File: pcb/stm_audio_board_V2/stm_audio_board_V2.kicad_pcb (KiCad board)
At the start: 4 copper layers, 141 parts, among them J1 Power conn, J10 Conn_01x03_taptempo, J2 STlink, J3 Audio_sig, J4 Conn_01x10_pots_internal, J5 SPI, J6 Conn_01x03_pot_ext, J7 GuitarIN, J8 GuitarOUT_R, J9 GuitarOUT_L, SW1 SW_SPST, U1 STM32H730VBTx, U2 AMS1117-3.3, U4 OP275, U5 AMS1117-3.3, U7 MCP1703Ax-500xxDB, U9 L7809, Y1 Crystal_GND24, Y2 X1E0000210132

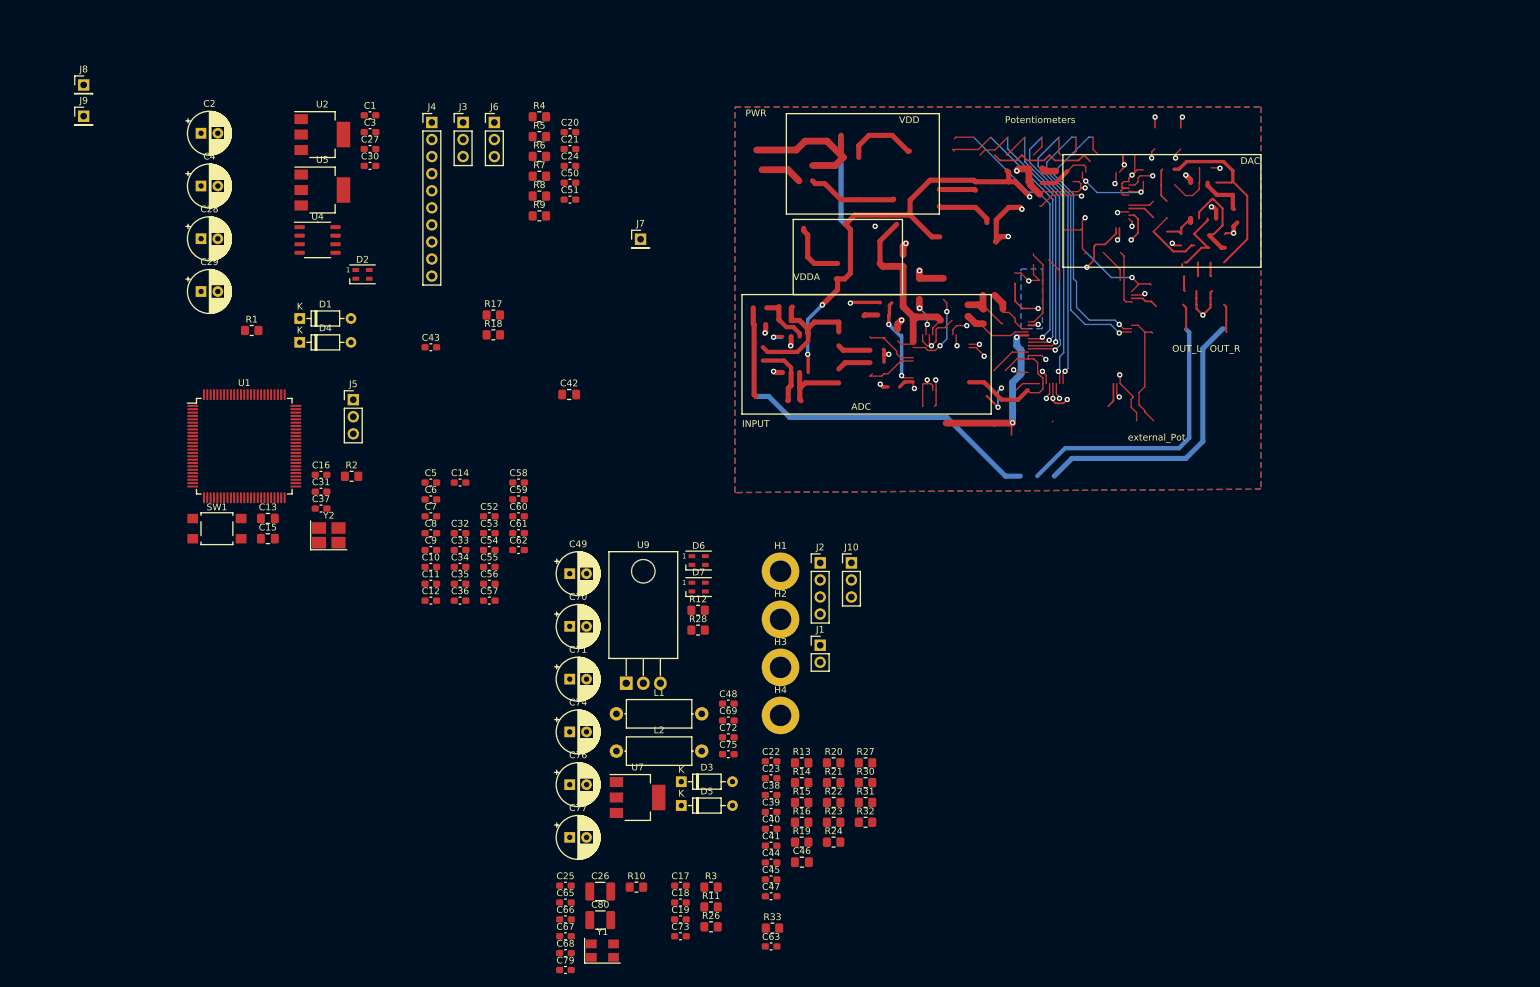
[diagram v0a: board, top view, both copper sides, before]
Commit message: PCB design started INPUT and OUTPUT stage done, codec placed
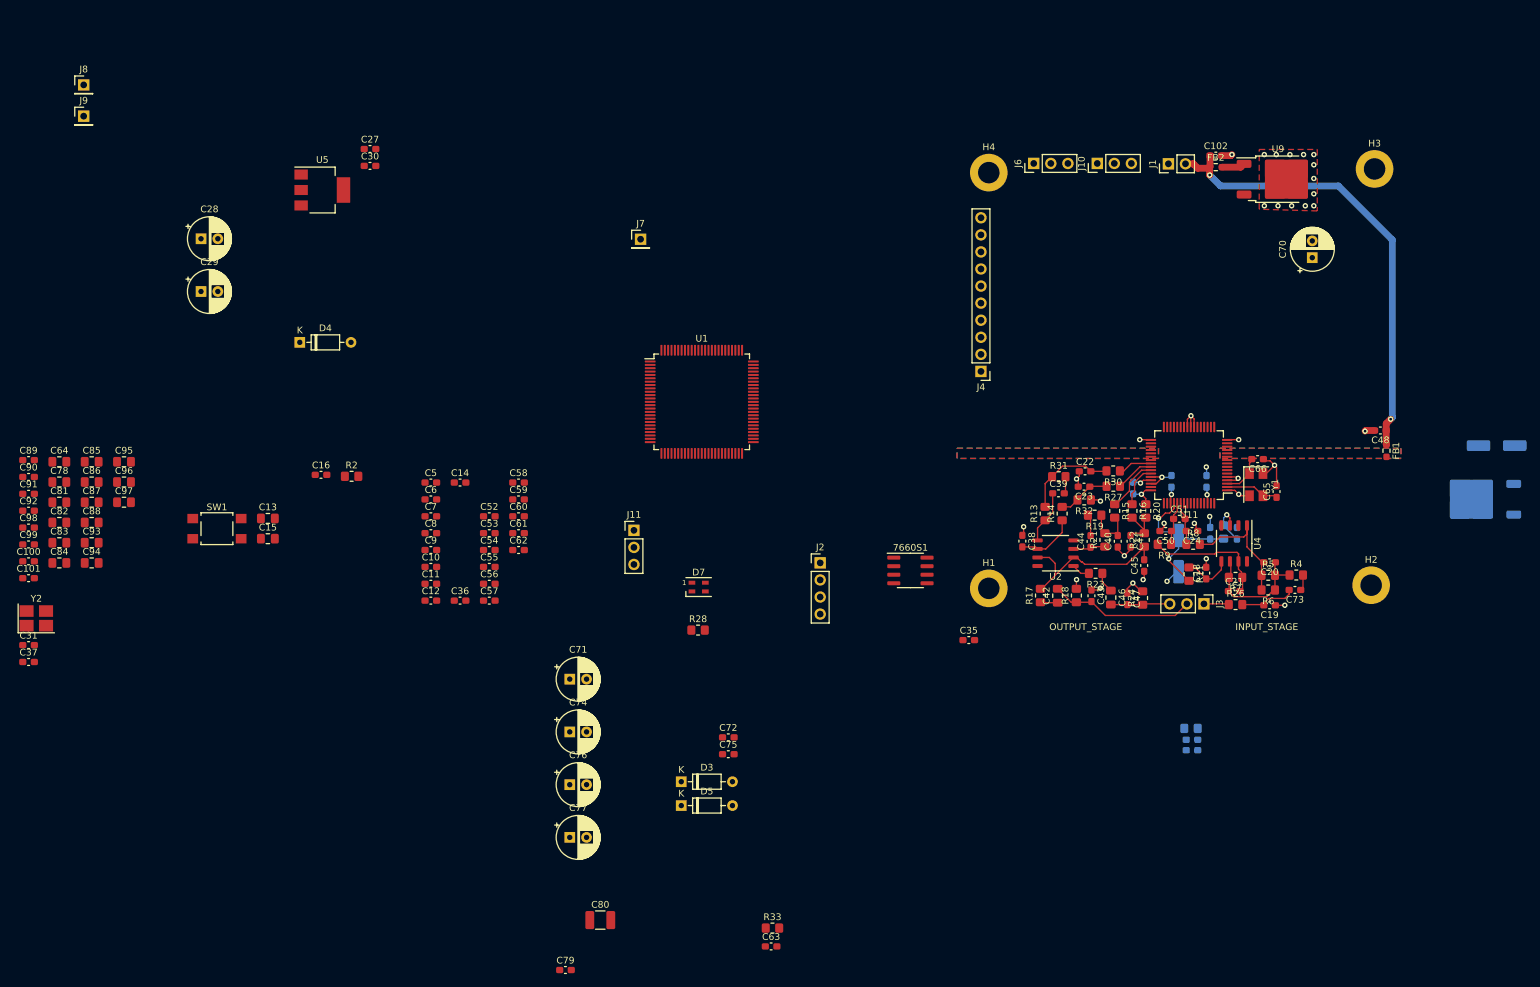
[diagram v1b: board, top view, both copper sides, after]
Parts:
- removed C1, C3, C69: 100nF, Capacitor_SMD:C_0603_1608Metric_Pad1.08x0.95mm_HandSolder
- removed C2: 1uF, Capacitor_THT:CP_Radial_D6.3mm_P2.50mm
- removed C4: 100uF, Capacitor_THT:CP_Radial_D6.3mm_P2.50mm
- removed D1: 1N4148, Diode_THT:D_DO-35_SOD27_P7.62mm_Horizontal
- removed D2, D6: LED, LED_SMD:LED_SK6805_PLCC4_2.4x2.7mm_P1.3mm
- removed J5: SPI, Connector_PinHeader_2.54mm:PinHeader_1x03_P2.54mm_Vertical
- removed L1, L2: 10 uH|0,5R, Inductor_THT:L_Axial_L9.5mm_D4.0mm_P12.70mm_Horizontal_Fastron_SMCC
- removed R1: 330R, Resistor_SMD:R_0805_2012Metric_Pad1.20x1.40mm_HandSolder
- removed R12: 10k, Resistor_SMD:R_0805_2012Metric_Pad1.20x1.40mm_HandSolder
- removed U7: MCP1703Ax-500xxDB, Package_TO_SOT_SMD:SOT-223-3_TabPin2
- added 7660S1: ~, Package_SO:SOIC-8_3.9x4.9mm_P1.27mm, F.Cu at (175.9, 109.6)
- added C100: 100nF, Capacitor_SMD:C_0603_1608Metric_Pad1.08x0.95mm_HandSolder, F.Cu at (44.7, 108.3)
- added C101: 100nF, Capacitor_SMD:C_0603_1608Metric_Pad1.08x0.95mm_HandSolder, F.Cu at (44.7, 110.8)
- added C102: 100nF, Capacitor_SMD:C_0603_1608Metric_Pad1.08x0.95mm_HandSolder, F.Cu at (221.4, 47.9)
- added C64: 47uF, Capacitor_SMD:C_0805_2012Metric_Pad1.18x1.45mm_HandSolder, F.Cu at (49.3, 93.5)
- added C78: 47uF, Capacitor_SMD:C_0805_2012Metric_Pad1.18x1.45mm_HandSolder, F.Cu at (49.3, 96.5)
- added C81: 47uF, Capacitor_SMD:C_0805_2012Metric_Pad1.18x1.45mm_HandSolder, F.Cu at (49.3, 99.5)
- added C82: 47uF, Capacitor_SMD:C_0805_2012Metric_Pad1.18x1.45mm_HandSolder, F.Cu at (49.3, 102.5)
- added C83: 47uF, Capacitor_SMD:C_0805_2012Metric_Pad1.18x1.45mm_HandSolder, F.Cu at (49.3, 105.5)
- added C84: 47uF, Capacitor_SMD:C_0805_2012Metric_Pad1.18x1.45mm_HandSolder, F.Cu at (49.3, 108.5)
- added C85: 47uF, Capacitor_SMD:C_0805_2012Metric_Pad1.18x1.45mm_HandSolder, F.Cu at (54.1, 93.5)
- added C86: 47uF, Capacitor_SMD:C_0805_2012Metric_Pad1.18x1.45mm_HandSolder, F.Cu at (54.1, 96.5)
- added C87: 47uF, Capacitor_SMD:C_0805_2012Metric_Pad1.18x1.45mm_HandSolder, F.Cu at (54.1, 99.5)
- added C88: 47uF, Capacitor_SMD:C_0805_2012Metric_Pad1.18x1.45mm_HandSolder, F.Cu at (54.1, 102.5)
- added C89: 100nF, Capacitor_SMD:C_0603_1608Metric_Pad1.08x0.95mm_HandSolder, F.Cu at (44.7, 93.2)
- added C90: 100nF, Capacitor_SMD:C_0603_1608Metric_Pad1.08x0.95mm_HandSolder, F.Cu at (44.7, 95.7)
- added C91: 100nF, Capacitor_SMD:C_0603_1608Metric_Pad1.08x0.95mm_HandSolder, F.Cu at (44.7, 98.2)
- added C92: 100nF, Capacitor_SMD:C_0603_1608Metric_Pad1.08x0.95mm_HandSolder, F.Cu at (44.7, 100.7)
- added C93: 47uF, Capacitor_SMD:C_0805_2012Metric_Pad1.18x1.45mm_HandSolder, F.Cu at (54.1, 105.5)
- added C94: 47uF, Capacitor_SMD:C_0805_2012Metric_Pad1.18x1.45mm_HandSolder, F.Cu at (54.1, 108.5)
- added C95: 47uF, Capacitor_SMD:C_0805_2012Metric_Pad1.18x1.45mm_HandSolder, F.Cu at (58.9, 93.5)
- added C96: 47uF, Capacitor_SMD:C_0805_2012Metric_Pad1.18x1.45mm_HandSolder, F.Cu at (58.9, 96.5)
- added C97: 47uF, Capacitor_SMD:C_0805_2012Metric_Pad1.18x1.45mm_HandSolder, F.Cu at (58.9, 99.5)
- added C98: 100nF, Capacitor_SMD:C_0603_1608Metric_Pad1.08x0.95mm_HandSolder, F.Cu at (44.7, 103.3)
- added C99: 100nF, Capacitor_SMD:C_0603_1608Metric_Pad1.08x0.95mm_HandSolder, F.Cu at (44.7, 105.8)
- added FB1: FerriteBead, Resistor_SMD:R_0603_1608Metric_Pad0.98x0.95mm_HandSolder, F.Cu at (246.8, 91.8)
- added FB2: FerriteBead, Resistor_SMD:R_0603_1608Metric_Pad0.98x0.95mm_HandSolder, F.Cu at (221.4, 49.6)
- added J11: SPI, Connector_PinHeader_2.54mm:PinHeader_1x03_P2.54mm_Vertical, F.Cu at (134.8, 103.7)
- added U11: ~, Package_QFP:LQFP-64_10x10mm_P0.5mm, F.Cu at (217.4, 94.0)
- added U8: L78M09CDT, Package_TO_SOT_SMD:TO-252-2, B.Cu at (260.7, 99.0)
- C17, C25, C32, C33, C34, C67, C68, R10, R3: moved to B.Cu
- C26: footprint Capacitor_SMD:C_1210_3225Metric_Pad1.33x2.70mm_HandSolder -> Capacitor_SMD:CP_Elec_6.3x7.7; moved to B.Cu
- C49: footprint Capacitor_THT:CP_Radial_D6.3mm_P2.50mm -> Capacitor_SMD:CP_Elec_6.3x7.7; moved to B.Cu
- C71, C74: value 1uF -> 47uf
- U2: value AMS1117-3.3 -> OP275; footprint Package_TO_SOT_SMD:SOT-223-3_TabPin2 -> Package_SO:SSOP-8_3.9x5.05mm_P1.27mm
- U9: value L7809 -> LF33_TO252; footprint Package_TO_SOT_THT:TO-220-3_Horizontal_TabDown -> Package_TO_SOT_SMD:TO-252-2
- moved U4 143.7 mm to (224.1, 105.6), turned to -90 degrees
- moved C49 139.2 mm to (263.2, 91.1), turned to 180 degrees
- moved R4 131.7 mm to (233.4, 110.3)
- moved J3 131.5 mm to (219.6, 114.6), turned to -90 degrees
- moved R5 126.6 mm to (229.2, 110.4)
- moved R6 126.2 mm to (229.2, 112.5), turned to 180 degrees
- moved U2 125.6 mm to (197.5, 107.1), turned to 180 degrees
- moved C66 123.7 mm to (227.6, 93.1), turned to 180 degrees
- moved C70 123.4 mm to (235.7, 63.1), turned to 90 degrees
- moved U9 122.6 mm to (230.6, 51.4)
- moved C20 122.2 mm to (229.4, 108.4), turned to 180 degrees
- moved C65 122.2 mm to (230.4, 97.9), turned to 90 degrees
- moved R7 119.6 mm to (224.3, 110.7), turned to 180 degrees
- moved Y1 119.5 mm to (227.4, 96.9), turned to -90 degrees
- moved C21 118.7 mm to (224.1, 112.7)
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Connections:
- C27 pad 1: Net-(D4-K) -> +9V
- C28 pad 1: Net-(D4-K) -> +9V
- C31 pad 2: Net-(U1-PH0) -> OSC0
- C32 pad 2: GNDA -> GND
- C33 pad 2: GNDA -> GND
- C34 pad 2: GNDA -> GND
- C35 pad 2: GNDA -> GND
- C36 pad 2: GNDA -> GND
- C37 pad 2: Net-(U1-PH1) -> OSC1
- C38 pad 2: Net-(U6A--) -> Net-(U2B--)
- C39 pad 1: Net-(U6A-+) -> Net-(U2B-+)
- C44 pad 1: Net-(U3B-+) -> Net-(U2A-+)
- C45 pad 2: Net-(U3B--) -> Net-(U2A--)
- C48 pad 1: Net-(D3-K) -> PWR_INPUT_12V-18V
- C52 pad 2: GNDA -> GND
- C53 pad 2: GNDA -> GND
- C70 pad 1: +9V -> Net-(D5-K)
- C71 pad 1: +5V -> +3.3V
- C72 pad 1: +5V -> +3.3V
- D4 pad 1: Net-(D4-K) -> +9V
- D5 pad 1: +9V -> Net-(D5-K)
- D5 pad 2: +5V -> +3.3V
- J1 pad 2: PWR_INPUT_9-18V -> PWR_INPUT_12V-18V
- R13 pad 1: Net-(U6A-+) -> Net-(U2B-+)
- R14 pad 1: Net-(U6A--) -> Net-(U2B--)
- R21 pad 1: Net-(U3B-+) -> Net-(U2A-+)
- R22 pad 1: Net-(U3B--) -> Net-(U2A--)
- U1 pad 12: Net-(U1-PH0) -> OSC0
- U1 pad 13: Net-(U1-PH1) -> OSC1
- U2 pad 1: GND -> Net-(R23-Pad2)
- U2 pad 2: +3.3V -> Net-(U2A--)
- U2 pad 3: +5V -> Net-(U2A-+)
- U5 pad 3: Net-(D4-K) -> +9V
- U9 pad 1: Net-(D3-K) -> Net-(D5-K)
- U9 pad 3: +9V -> +3.3V
- Y2 pad 1: Net-(U1-PH1) -> OSC0
- Y2 pad 3: Net-(U1-PH0) -> OSC1
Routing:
- net (no net): track 1249.0 -> 0.00 mm, vias 42 -> 0
- net VDD: track 155.2 -> 0.00 mm, vias 7 -> 0
- net GNDA: track 82.4 -> 0.00 mm, vias 20 -> 0
- net PWR_INPUT_12V-18V: track 0.00 -> 68.9 mm, vias 0 -> 2
- net +3.3VA: track 63.6 -> 7.52 mm, vias 6 -> 3
- net AD1939_CM: track 0.00 -> 24.5 mm, vias 0 -> 2
- net GUITAR_OUT_L/MONO: track 0.00 -> 21.7 mm
- net Net-(C40-Pad2): track 28.3 -> 7.33 mm
- net Net-(C20-Pad2): track 0.00 -> 19.7 mm
- net Net-(C21-Pad2): track 0.00 -> 18.4 mm
- net GND: track 80.1 -> 64.6 mm, vias 6 -> 38
- net Net-(C22-Pad2): track 0.00 -> 14.0 mm
- net Net-(U2A--): track 0.00 -> 13.4 mm
- net Net-(R17-Pad2): track 0.00 -> 11.9 mm
- net Net-(U1-PH1): track 10.2 -> 0.00 mm
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- added copper zone on B.Cu, net (none)
- added copper zone on F.Cu, net (none)
- added copper zone on In1.Cu, net (none)
- added copper zone on In2.Cu, net (none)
- added copper zone on In1.Cu, net GND
- removed copper zone on In2.Cu, net +3.3VA
- removed copper zone on B.Cu, net GNDA
- removed copper zone on B.Cu, net VDD
- removed copper zone on In1.Cu, net VDD
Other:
- board text added: "INPUT_STAGE"
- board text added: "OUTPUT_STAGE"
- board text removed: "ADC"
- board text removed: "DAC"
- board text removed: "INPUT"
- board text removed: "OUT_L"
- board text removed: "OUT_R"
- board text removed: "PWR"
- board text removed: "Potentiometers"
- board text removed: "VDD"
- board text removed: "VDDA"
- board text removed: "external_Pot"

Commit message: Update #auto_saved_files#, Connectors.kicad_sch, and 18 more files...
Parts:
- removed C100, C101, C35, C36, C52, C53, C91, C92, C98, C99: 100nF, Capacitor_SMD:C_0603_1608Metric_Pad1.08x0.95mm_HandSolder
- removed C84, C85, C86, C87, C88, C93, C94, C95, C96, C97: 47uF, Capacitor_SMD:C_0805_2012Metric_Pad1.18x1.45mm_HandSolder
- removed D4: 1N4148, Diode_THT:D_DO-35_SOD27_P7.62mm_Horizontal
- removed J7: GuitarIN, Connector_PinHeader_2.54mm:PinHeader_1x01_P2.54mm_Vertical
- removed J8: GuitarOUT_R, Connector_PinHeader_2.54mm:PinHeader_1x01_P2.54mm_Vertical
- removed J9: GuitarOUT_L, Connector_PinHeader_2.54mm:PinHeader_1x01_P2.54mm_Vertical
- C10, C11, C14, C15, C40, C41, C44, C45, C46, C47, C48, C6, C65, C66, C7, C76, C77, C79, C80, C9, FB1, R15, R16, R19, R2, R20, R21, R22, R23, R24, Y1: moved to B.Cu
- C28, C29: footprint Capacitor_THT:CP_Radial_D6.3mm_P2.50mm -> Capacitor_SMD:CP_Elec_6.3x7.7; moved to B.Cu
- C49: footprint Capacitor_SMD:CP_Elec_6.3x7.7 -> Capacitor_SMD:C_1206_3216Metric_Pad1.33x1.80mm_HandSolder
- moved C83 193.7 mm to (242.3, 88.3), turned to 90 degrees
- moved C82 190.5 mm to (239.3, 88.3), turned to 90 degrees
- moved C81 187.3 mm to (236.2, 88.3), turned to 90 degrees
- moved C90 185.0 mm to (229.4, 106.4)
- moved C78 184.1 mm to (233.2, 88.3), turned to 90 degrees
- moved C64 181.0 mm to (230.2, 88.3), turned to 90 degrees
- moved C31 165.2 mm to (200.2, 64.9)
- moved Y2 162.6 mm to (201.1, 68.4), turned to 180 degrees
- moved C37 161.8 mm to (197.1, 68.9), turned to -90 degrees
- moved C89 156.1 mm to (199.9, 110.2), turned to 90 degrees
- moved C13 148.6 mm to (224.6, 66.3)
- moved C15 142.1 mm to (219.0, 73.9)
- moved C12 130.2 mm to (224.1, 62.5), turned to -90 degrees
- moved C29 129.3 mm to (193.8, 106.7), turned to 180 degrees
- moved C74 127.2 mm to (250.2, 109.8)
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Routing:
- net +9V: track 0.00 -> 124.8 mm, vias 0 -> 4
- net +3.3V: track 0.00 -> 119.5 mm, vias 0 -> 7
- net GND: track 64.6 -> 147.1 mm, vias 38 -> 86
- net +3.3VA: track 7.52 -> 57.8 mm, vias 3 -> 4
- net -9V: track 0.00 -> 40.2 mm, vias 0 -> 2
- net /MCU/NRST: track 0.00 -> 33.6 mm, vias 0 -> 2
- net CLK: track 0.00 -> 31.0 mm, vias 0 -> 1
- net SWCLK: track 0.00 -> 31.0 mm, vias 0 -> 2
- net MISO: track 0.00 -> 26.7 mm, vias 0 -> 1
- net MOSI: track 0.00 -> 26.4 mm, vias 0 -> 1
- net SWDIO: track 0.00 -> 26.2 mm, vias 0 -> 1
- net DAC_EN: track 0.00 -> 17.3 mm
- net Net-(D5-K): track 3.50 -> 17.1 mm
- net AD1939_LF: track 0.00 -> 10.5 mm, vias 0 -> 1
- net AD1939_FILTR: track 0.00 -> 10.1 mm, vias 0 -> 1
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- added copper zone on B.Cu, net GND
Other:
- board text added: "U8"

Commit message: trace widening
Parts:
- added C100: 100nF, Capacitor_SMD:C_0603_1608Metric_Pad1.08x0.95mm_HandSolder, F.Cu at (153.1, 83.3)
- added C101: 100nF, Capacitor_SMD:C_0603_1608Metric_Pad1.08x0.95mm_HandSolder, F.Cu at (153.1, 85.8)
- added C35: 100nF, Capacitor_SMD:C_0603_1608Metric_Pad1.08x0.95mm_HandSolder, F.Cu at (153.1, 63.2)
- added C36: 100nF, Capacitor_SMD:C_0603_1608Metric_Pad1.08x0.95mm_HandSolder, F.Cu at (153.1, 65.7)
- added C52: 100nF, Capacitor_SMD:C_0603_1608Metric_Pad1.08x0.95mm_HandSolder, F.Cu at (153.1, 68.3)
- added C53: 100nF, Capacitor_SMD:C_0603_1608Metric_Pad1.08x0.95mm_HandSolder, F.Cu at (153.1, 70.8)
- added C84: 47uF, Capacitor_SMD:C_0805_2012Metric_Pad1.18x1.45mm_HandSolder, F.Cu at (157.6, 63.5)
- added C85: 47uF, Capacitor_SMD:C_0805_2012Metric_Pad1.18x1.45mm_HandSolder, F.Cu at (157.6, 66.5)
- added C86: 47uF, Capacitor_SMD:C_0805_2012Metric_Pad1.18x1.45mm_HandSolder, F.Cu at (157.6, 69.5)
- added C87: 47uF, Capacitor_SMD:C_0805_2012Metric_Pad1.18x1.45mm_HandSolder, F.Cu at (157.6, 72.5)
- added C88: 47uF, Capacitor_SMD:C_0805_2012Metric_Pad1.18x1.45mm_HandSolder, F.Cu at (157.6, 75.5)
- added C91: 100nF, Capacitor_SMD:C_0603_1608Metric_Pad1.08x0.95mm_HandSolder, F.Cu at (153.1, 73.3)
- added C92: 100nF, Capacitor_SMD:C_0603_1608Metric_Pad1.08x0.95mm_HandSolder, F.Cu at (153.1, 75.8)
- added C93: 47uF, Capacitor_SMD:C_0805_2012Metric_Pad1.18x1.45mm_HandSolder, F.Cu at (162.4, 63.5)
- added C94: 47uF, Capacitor_SMD:C_0805_2012Metric_Pad1.18x1.45mm_HandSolder, F.Cu at (162.4, 66.5)
- added C95: 47uF, Capacitor_SMD:C_0805_2012Metric_Pad1.18x1.45mm_HandSolder, F.Cu at (162.4, 69.5)
- added C96: 47uF, Capacitor_SMD:C_0805_2012Metric_Pad1.18x1.45mm_HandSolder, F.Cu at (162.4, 72.5)
- added C97: 47uF, Capacitor_SMD:C_0805_2012Metric_Pad1.18x1.45mm_HandSolder, F.Cu at (162.4, 75.5)
- added C98: 100nF, Capacitor_SMD:C_0603_1608Metric_Pad1.08x0.95mm_HandSolder, F.Cu at (153.1, 78.3)
- added C99: 100nF, Capacitor_SMD:C_0603_1608Metric_Pad1.08x0.95mm_HandSolder, F.Cu at (153.1, 80.8)
- added U3: STM32H747AIIx, Package_BGA:UFBGA-169_7x7mm_Layout13x13_P0.5mm, F.Cu at (174.9, 69.5)
- C28, C29: footprint Capacitor_SMD:CP_Elec_6.3x7.7 -> Capacitor_Tantalum_SMD:CP_EIA-7343-31_Kemet-D_Pad2.25x2.55mm_HandSolder
- C76, C77: footprint Capacitor_THT:CP_Radial_D6.3mm_P2.50mm -> Capacitor_Tantalum_SMD:CP_EIA-7343-31_Kemet-D_Pad2.25x2.55mm_HandSolder
- moved C77 2.59 mm to (236.0, 107.7)
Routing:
- net +9V: track 124.8 -> 106.8 mm, vias 4 -> 5
- net Net-(U4A--): track 6.42 -> 15.5 mm
- net -9V: track 40.2 -> 49.1 mm, vias 2 -> 3
- net GND: track 147.1 -> 152.7 mm
- net +3.3VA: track 57.8 -> 62.9 mm, vias 4 -> 3
- net AD1939_CM: track 24.5 -> 27.8 mm
- net Net-(R17-Pad2): track 5.20 -> 6.39 mm
- net GUITAR_OUT_L/MONO: track 13.2 -> 14.2 mm
- net Net-(C20-Pad2): track 19.6 -> 20.5 mm
- net Net-(C22-Pad2): track 9.90 -> 10.6 mm
- removed copper zone on B.Cu, net (none)
- removed copper zone on F.Cu, net (none)
- removed copper zone on In1.Cu, net (none)
- removed copper zone on In2.Cu, net (none)

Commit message: saving
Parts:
- added C1: 2.2uF, Capacitor_SMD:C_0805_2012Metric_Pad1.18x1.45mm_HandSolder, F.Cu at (170.7, 79.4)
- added C2: 2.2uF, Capacitor_SMD:C_0805_2012Metric_Pad1.18x1.45mm_HandSolder, F.Cu at (170.7, 82.4)
- added R1: 10k, Resistor_SMD:R_0805_2012Metric_Pad1.20x1.40mm_HandSolder, F.Cu at (170.7, 85.3)
- added U1: STM32H747IGTx, Package_QFP:LQFP-176_24x24mm_P0.5mm, F.Cu at (166.4, 42.2)
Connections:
- U3 pad A1: Net-(U3-VSS-PadA1) -> GND
- U3 pad A11: unconnected-(U3-PA14-PadA11) -> SWCLK
- U3 pad A12: Net-(U3-VSS-PadA1) -> GND
- U3 pad A3: unconnected-(U3-VDDLDO-PadA3) -> +3.3V
- U3 pad A4: unconnected-(U3-VCAP-PadA4) -> Net-(C1-Pad1)
- U3 pad A7: Net-(U3-VSS-PadA1) -> GND
- U3 pad A9: unconnected-(U3-VDD-PadA9) -> +3.3V
- U3 pad B1: unconnected-(U3-VBAT-PadB1) -> +3.3V
- U3 pad B11: unconnected-(U3-PA13-PadB11) -> SWDIO
- U3 pad B12: unconnected-(U3-VDD-PadB12) -> +3.3V
- U3 pad B13: unconnected-(U3-VDDLDO-PadB13) -> +3.3V
- U3 pad B2: unconnected-(U3-VDD-PadB2) -> +3.3V
- U3 pad B4: Net-(U3-VSS-PadA1) -> GND
- U3 pad B5: unconnected-(U3-BOOT0-PadB5) -> Net-(U3-BOOT0)
- U3 pad B7: unconnected-(U3-VDD-PadB7) -> +3.3V
- U3 pad B9: Net-(U3-VSS-PadA1) -> GND
- U3 pad C12: Net-(U3-VSS-PadA1) -> GND
- U3 pad C13: unconnected-(U3-VCAP-PadC13) -> Net-(C1-Pad1)
- U3 pad D1: Net-(U3-VSS-PadA1) -> GND
- U3 pad E12: unconnected-(U3-VDD-PadE12) -> +3.3V
- U3 pad E13: Net-(U3-VSS-PadA1) -> GND
- U3 pad E2: unconnected-(U3-VDD-PadE2) -> +3.3V
- U3 pad F1: unconnected-(U3-VDDSMPS-PadF1) -> GND
- U3 pad F12: unconnected-(U3-VDD50_USB-PadF12) -> +3.3V
- U3 pad F13: unconnected-(U3-VDD33_USB-PadF13) -> +3.3V
- U3 pad F2: unconnected-(U3-VSSSMPS-PadF2) -> GND
- U3 pad F3: unconnected-(U3-VFBSMPS-PadF3) -> GND
- U3 pad G12: Net-(U3-VSSDSI-PadG12) -> GND
- U3 pad G13: Net-(U3-VSSDSI-PadG12) -> GND
- U3 pad H1: unconnected-(U3-VDD-PadH1) -> +3.3V
- U3 pad H11: Net-(U3-VSS-PadA1) -> GND
- U3 pad H2: Net-(U3-VSS-PadA1) -> GND
- U3 pad H5: unconnected-(U3-NRST-PadH5) -> /MCU/NRST
- U3 pad J1: unconnected-(U3-PH1-PadJ1) -> OSC1
- U3 pad J11: Net-(U3-VSS-PadA1) -> GND
- U3 pad J2: unconnected-(U3-PH0-PadJ2) -> OSC0
- U3 pad J5: unconnected-(U3-PA5-PadJ5) -> CLK
- U3 pad K11: Net-(U3-VSS-PadA1) -> GND
- U3 pad K4: unconnected-(U3-PA7-PadK4) -> MOSI
- U3 pad L1: unconnected-(U3-VREF--PadL1) -> GND
- U3 pad L11: unconnected-(U3-VDD-PadL11) -> +3.3V
- U3 pad L12: unconnected-(U3-VCAPDSI-PadL12) -> Net-(U3-VCAPDSI)
- U3 pad L13: Net-(U3-VSS-PadA1) -> GND
- U3 pad L2: unconnected-(U3-VDDA-PadL2) -> +3.3V
- U3 pad L9: unconnected-(U3-VDD-PadL9) -> +3.3V
- U3 pad M1: unconnected-(U3-VREF+-PadM1) -> +3.3V
- U3 pad M13: unconnected-(U3-VDDDSI-PadM13) -> +3.3V
- U3 pad M2: unconnected-(U3-VDD-PadM2) -> +3.3V
- U3 pad M4: unconnected-(U3-PA6-PadM4) -> MISO
- U3 pad M6: Net-(U3-VSS-PadA1) -> GND
- U3 pad M9: Net-(U3-VSS-PadA1) -> GND
- U3 pad N1: Net-(U3-VSS-PadA1) -> GND
- U3 pad N10: unconnected-(U3-VDDLDO-PadN10) -> +3.3V
- U3 pad N2: unconnected-(U3-PA3-PadN2) -> ADC_EN
- U3 pad N3: unconnected-(U3-PA4-PadN3) -> DAC_EN
- U3 pad N9: unconnected-(U3-VCAP-PadN9) -> Net-(C1-Pad1)
